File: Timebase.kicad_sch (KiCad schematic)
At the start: 57 parts

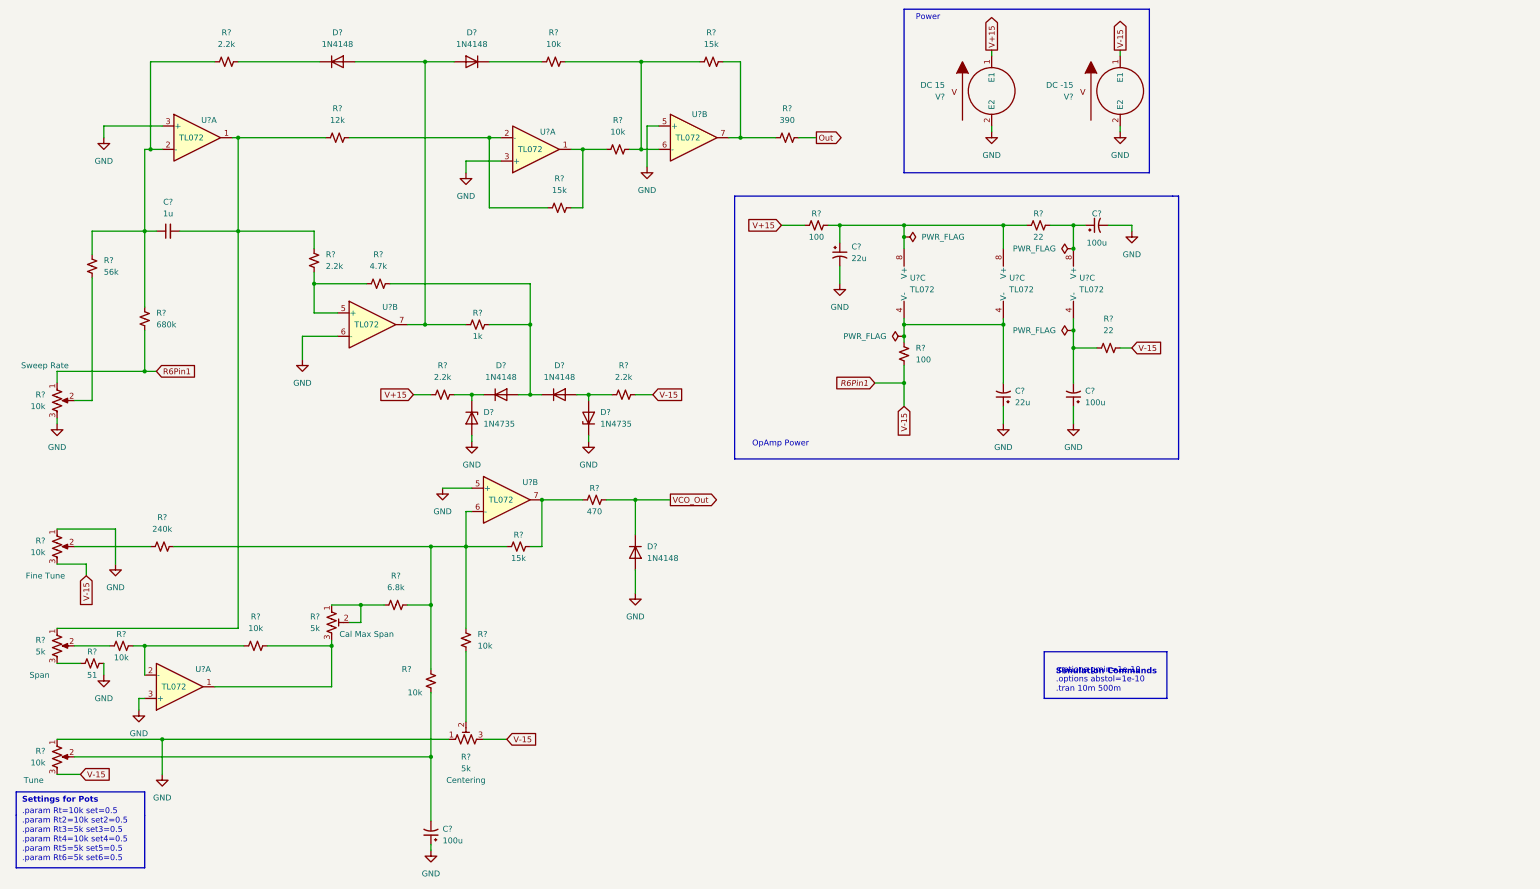
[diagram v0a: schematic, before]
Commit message: timebase pcb routed
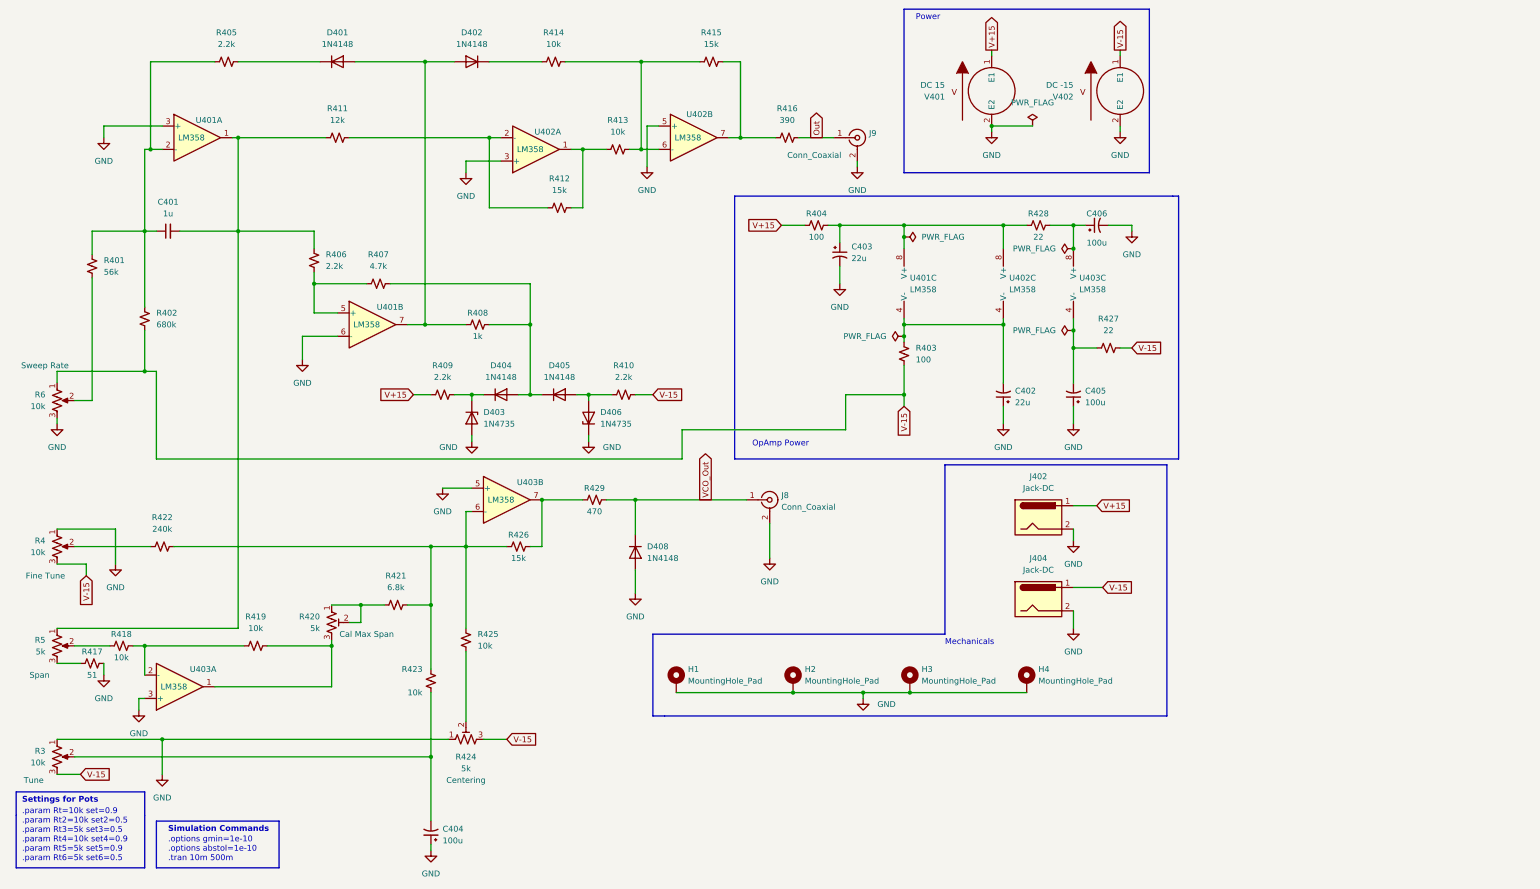
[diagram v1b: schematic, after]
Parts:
- added H1, H2, H3, H4: MountingHole_Pad, MountingHole:MountingHole_2.7mm_M2.5_DIN965_Pad_TopOnly, symbol Mechanical:MountingHole_Pad
- added J402, J404: Jack-DC, SnapEDA Library:CUI_PJ-007, symbol Connector:Jack-DC
- added J8, J9: Conn_Coaxial, SnapEDA Library:TE_5-1634503-1, symbol Connector:Conn_Coaxial
- C401: renamed from C?; footprint (none) -> Capacitor_THT:C_Radial_D4.0mm_H5.0mm_P1.50mm
- C402, C403, C404, C405, C406: renamed from C?; footprint (none) -> Capacitor_THT:CP_Axial_L11.0mm_D6.0mm_P18.00mm_Horizontal
- D403, D406: renamed from D?; footprint (none) -> Diode_THT:D_DO-35_SOD27_P7.62mm_Horizontal
- R3, R4, R5, R6: renamed from R?; footprint (none) -> Connector_Wire:SolderWire-0.127sqmm_1x03_P3.7mm_D0.48mm_OD1mm
- R401, R402, R403, R404, R405, R406, R407, R408, R409, R410, R411, R412, R413, R414, R415, R416, R417, R418, R419, R421, R422, R423, R425, R426, R427, R428, R429: renamed from R?; footprint (none) -> Resistor_THT:R_Axial_DIN0207_L6.3mm_D2.5mm_P7.62mm_Horizontal
- R420: renamed from R?; footprint (none) -> Potentiometer_THT:Potentiometer_Bourns_3296W_Vertical; Spice_Lib_File Pot5.lib -> Pot6.lib; Spice_Model pot_lin5 -> pot_lin6
- R424: renamed from R?; footprint (none) -> Potentiometer_THT:Potentiometer_Bourns_3296W_Vertical; Spice_Lib_File Pot6.lib -> Pot5.lib; Spice_Model pot_lin6 -> pot_lin5
- U401, U402, U403: renamed from U?; value TL072 -> LM358; footprint (none) -> SnapEDA Library:DIP794W45P254L959H508Q8; symbol Amplifier_Operational:TL072 -> Amplifier_Operational:LM358
- V401, V402: renamed from V?; footprint (none) -> SnapEDA Library:CUI_PJ-009A
- gave numbers to parts that had none: 5
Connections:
- net GND: now also H1.1, H2.1, H3.1, H4.1, J402.2, J404.2, J8.2 (Ext), J9.2 (Ext)
- net Out: now also J9.1 (In)
- net V+15: now also J402.1
- net VCO_Out: now also J8.1 (In)
- net R6Pin1 renamed V-15
- net V-15: now also J404.1
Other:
- note added: ".param Rt=10k set=0.9 .param Rt2=10k set2=0.5 .param Rt3=5k set3=0.5 .param Rt4=10k set4=0.9 .param Rt5=5k set5=0.9 .param Rt6=5k set6=0.5"
- note added: "Mechanicals"
- note removed: ".param Rt=10k set=0.5 .param Rt2=10k set2=0.5 .param Rt3=5k set3=0.5 .param Rt4=10k set4=0.5 .param Rt5=5k set5=0.5 .param Rt6=5k set6=0.5"
- company: (none) -> Andy McCann KA3KAF and Doug McCann KA3KAG
- title: (none) -> Spectrum Analyzer

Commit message: IF and log amp added
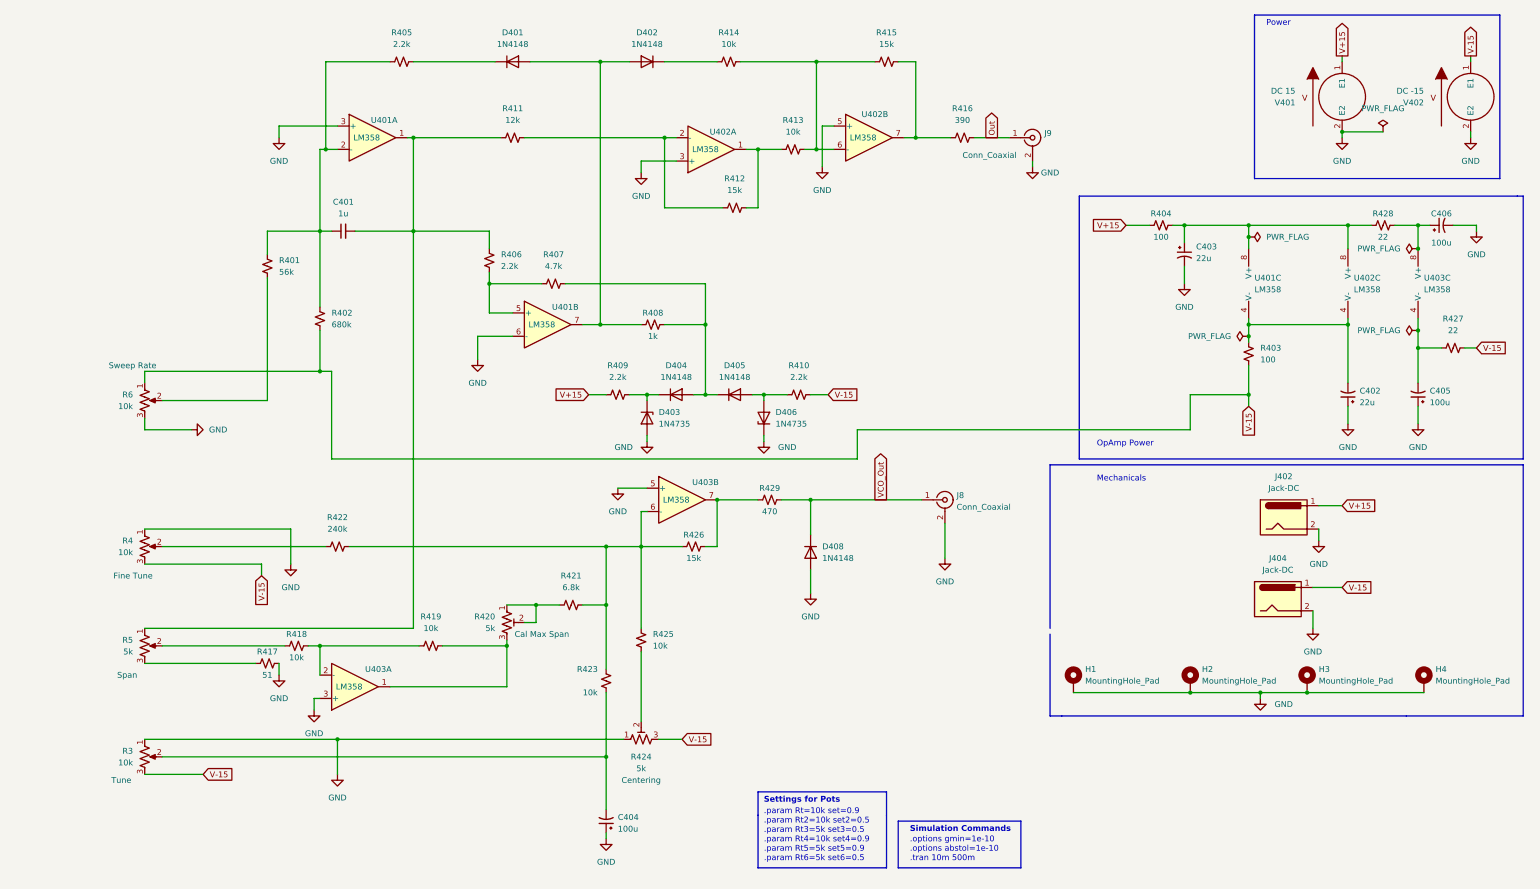
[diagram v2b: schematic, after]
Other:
- moved on the sheet: C401, C402, C403, C404, C405, C406, D401, D402, D403, D404, D405, D406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

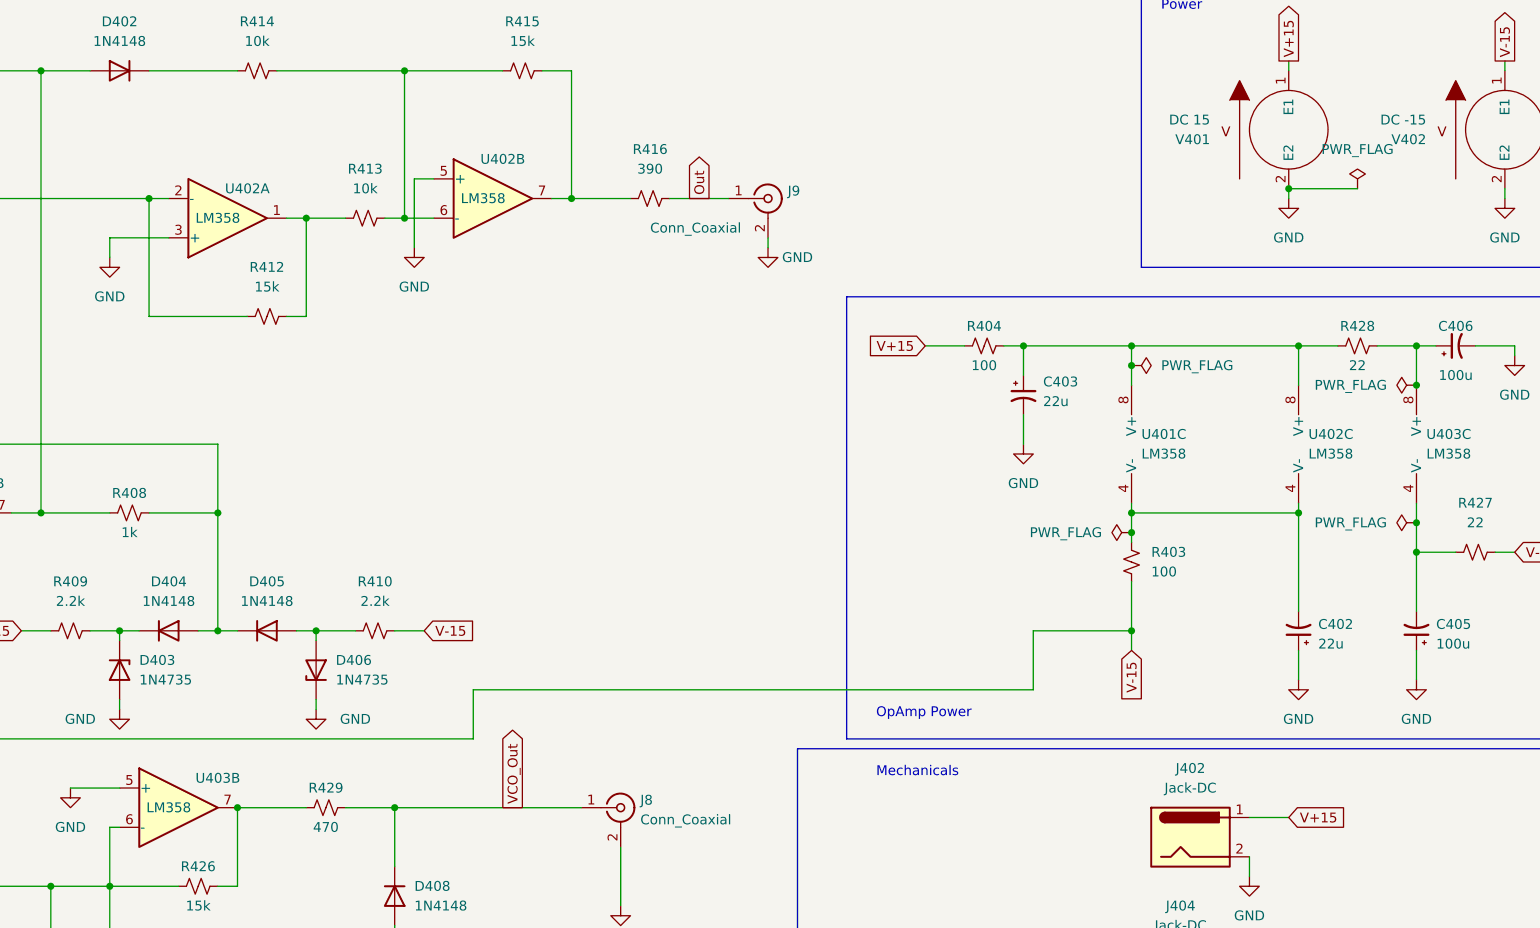
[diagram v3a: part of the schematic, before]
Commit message: Significant changes to timebase spice, 15v supply and resolution-filters
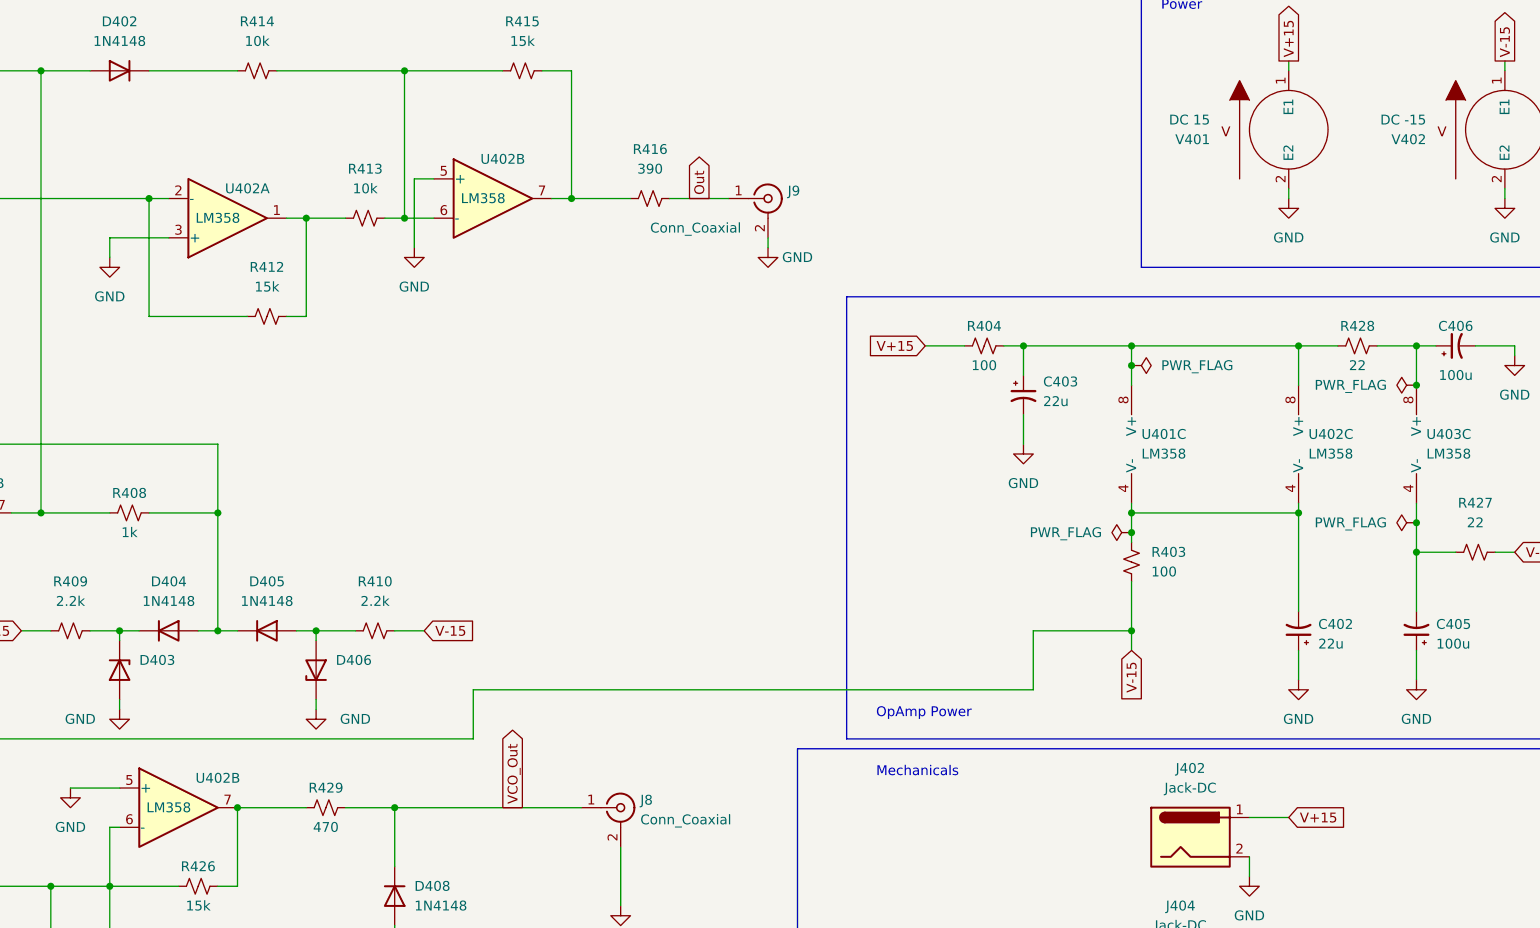
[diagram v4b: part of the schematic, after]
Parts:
- D403: value 1N4735 -> (none); footprint Diode_THT:D_DO-35_SOD27_P7.62mm_Horizontal -> (none)
- D406: value 1N4735 -> (none); footprint Diode_THT:D_DO-35_SOD27_P7.62mm_Horizontal -> (none); Spice_Node_Sequence (none) -> 2 1
- renumbered U403 to U402
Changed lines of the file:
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@@
   (junction (at 281.94 99.06) (diameter 0) (color 0 0 0 0)
   )
-  (junction (at 302.26 41.91) (diameter 0) (color 0 0 0 0)
-  )
   (junction (at 318.77 85.09) (diameter 0) (color 0 0 0 0)
   )
@@
   )
   (polyline (pts (xy 341.63 168.91) (xy 316.23 168.91))
-    (stroke (width 0) (type default) (color 0 0 0 0))
-  )
-  (wire (pts (xy 311.15 41.91) (xy 302.26 41.91))
     (stroke (width 0) (type default) (color 0 0 0 0))
   )
@@
     (pin "2")
   )
-  (symbol (lib_id "power:PWR_FLAG") (at 311.15 41.91 0) (unit 1)
-    (in_bom yes) (on_board yes) (fields_autoplaced)
-    (property "Reference" "#FLG05" (id 0) (at 311.15 40.005 0)
-      (effects (font (size 1.27 1.27)) hide)
-    )
-    (property "Value" "PWR_FLAG" (id 1) (at 311.15 36.83 0))
-    (property "Footprint" "" (id 2) (at 311.15 41.91 0)
-      (effects (font (size 1.27 1.27)) hide)
-    )
-    (property "Datasheet" "~" (id 3) (at 311.15 41.91 0)
-      (effects (font (size 1.27 1.27)) hide)
-    )
-    (pin "1")
-  )
   (symbol (lib_id "Mechanical:MountingHole_Pad") (at 320.04 161.29 0) (unit 1)
     (in_bom yes) (on_board yes) (fields_autoplaced)
@@
   (symbol (lib_id "Amplifier_Operational:LM358") (at 158.75 121.92 0) (unit 2)
     (in_bom yes) (on_board yes)
-    (property "Reference" "U403" (id 0) (at 163.83 118.11 0))
+    (property "Reference" "U402" (id 0) (at 163.83 118.11 0))
     (property "Value" "LM358" (id 1) (at 157.48 121.92 0))
     (property "Footprint" "SnapEDA Library:DIP794W45P254L959H508Q8" (id 2) (at 158.75 121.92 0)
@@
       (effects (font (size 1.27 1.27)) (justify left))
     )
-    (property "Value" "1N4735" (id 1) (at 153.67 105.4099 90)
-      (effects (font (size 1.27 1.27)) (justify left))
-    )
-    (property "Footprint" "Diode_THT:D_DO-35_SOD27_P7.62mm_Horizontal" (id 2) (at 151.13 104.14 0)
+    (property "Value" "" (id 1) (at 153.67 105.4099 90)
+      (effects (font (size 1.27 1.27)) (justify left))
+    )
+    (property "Footprint" "" (id 2) (at 151.13 104.14 0)
       (effects (font (size 1.27 1.27)) hide)
     )
@@
       (effects (font (size 1.27 1.27)) (justify right))
     )
-    (property "Value" "1N4735" (id 1) (at 179.07 105.4099 90)
+    (property "Value" "" (id 1) (at 179.07 105.4099 90)
       (effects (font (size 1.27 1.27)) (justify right))
     )
-    (property "Footprint" "Diode_THT:D_DO-35_SOD27_P7.62mm_Horizontal" (id 2) (at 176.53 104.14 0)
+    (property "Footprint" "" (id 2) (at 176.53 104.14 0)
       (effects (font (size 1.27 1.27)) hide)
     )
@@
       (effects (font (size 1.27 1.27)) hide)
     )
+    (property "Spice_Node_Sequence" "2 1" (id 8) (at 176.53 104.14 0)
+      (effects (font (size 1.27 1.27)) hide)
+    )

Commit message: if and log amp routing and 3d model
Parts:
- D403, D406: value (none) -> 1N4735; footprint (none) -> Diode_THT:D_DO-35_SOD27_P7.62mm_Horizontal
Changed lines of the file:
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@@
       (effects (font (size 1.27 1.27)) (justify left))
     )
-    (property "Value" "" (id 1) (at 153.67 105.4099 90)
+    (property "Value" "1N4735" (id 1) (at 153.67 105.4099 90)
       (effects (font (size 1.27 1.27)) (justify left))
     )
-    (property "Footprint" "" (id 2) (at 151.13 104.14 0)
+    (property "Footprint" "Diode_THT:D_DO-35_SOD27_P7.62mm_Horizontal" (id 2) (at 151.13 104.14 0)
       (effects (font (size 1.27 1.27)) hide)
     )
@@
       (effects (font (size 1.27 1.27)) (justify right))
     )
-    (property "Value" "" (id 1) (at 179.07 105.4099 90)
+    (property "Value" "1N4735" (id 1) (at 179.07 105.4099 90)
       (effects (font (size 1.27 1.27)) (justify right))
     )
-    (property "Footprint" "" (id 2) (at 176.53 104.14 0)
+    (property "Footprint" "Diode_THT:D_DO-35_SOD27_P7.62mm_Horizontal" (id 2) (at 176.53 104.14 0)
       (effects (font (size 1.27 1.27)) hide)
     )
